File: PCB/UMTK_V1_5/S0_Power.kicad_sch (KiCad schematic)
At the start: 12 parts, among them J4 Power IN, J5 PJ-102BH, U4 LM2576HVS-5, U5 LD1117AS33TR

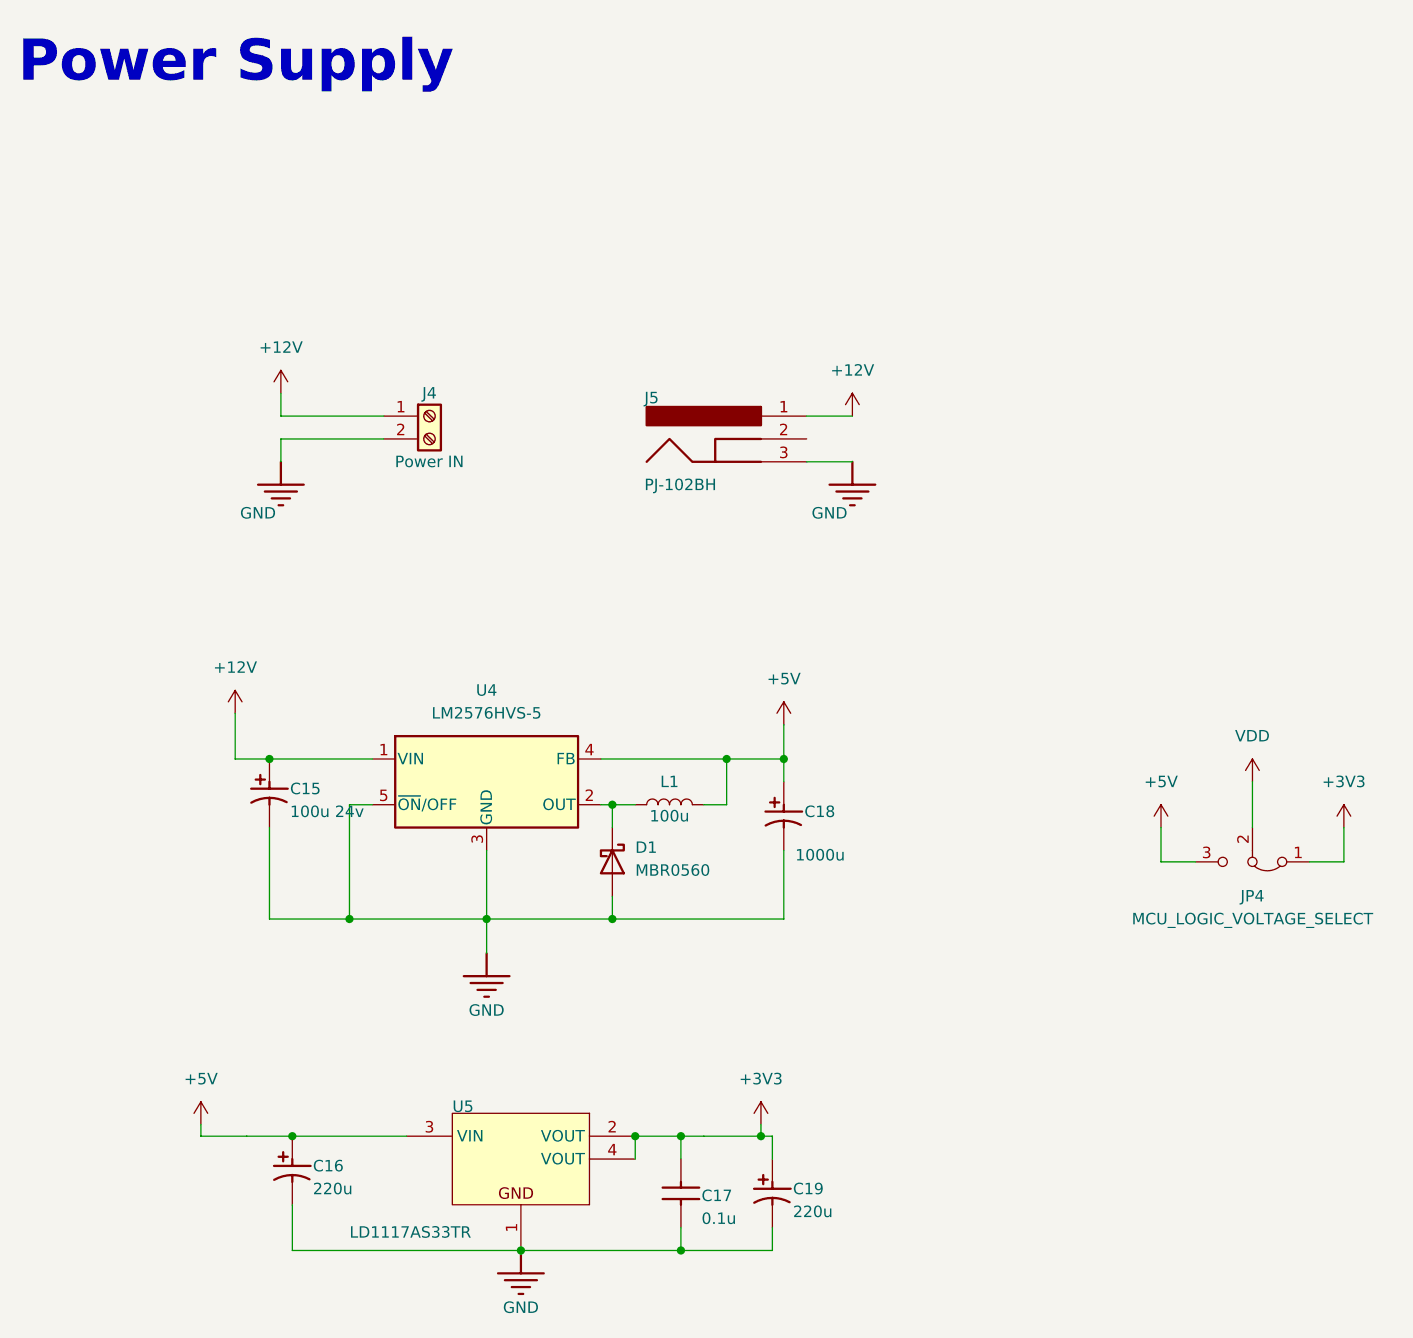
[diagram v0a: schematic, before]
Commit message: Schematic Done, Assigning footprint
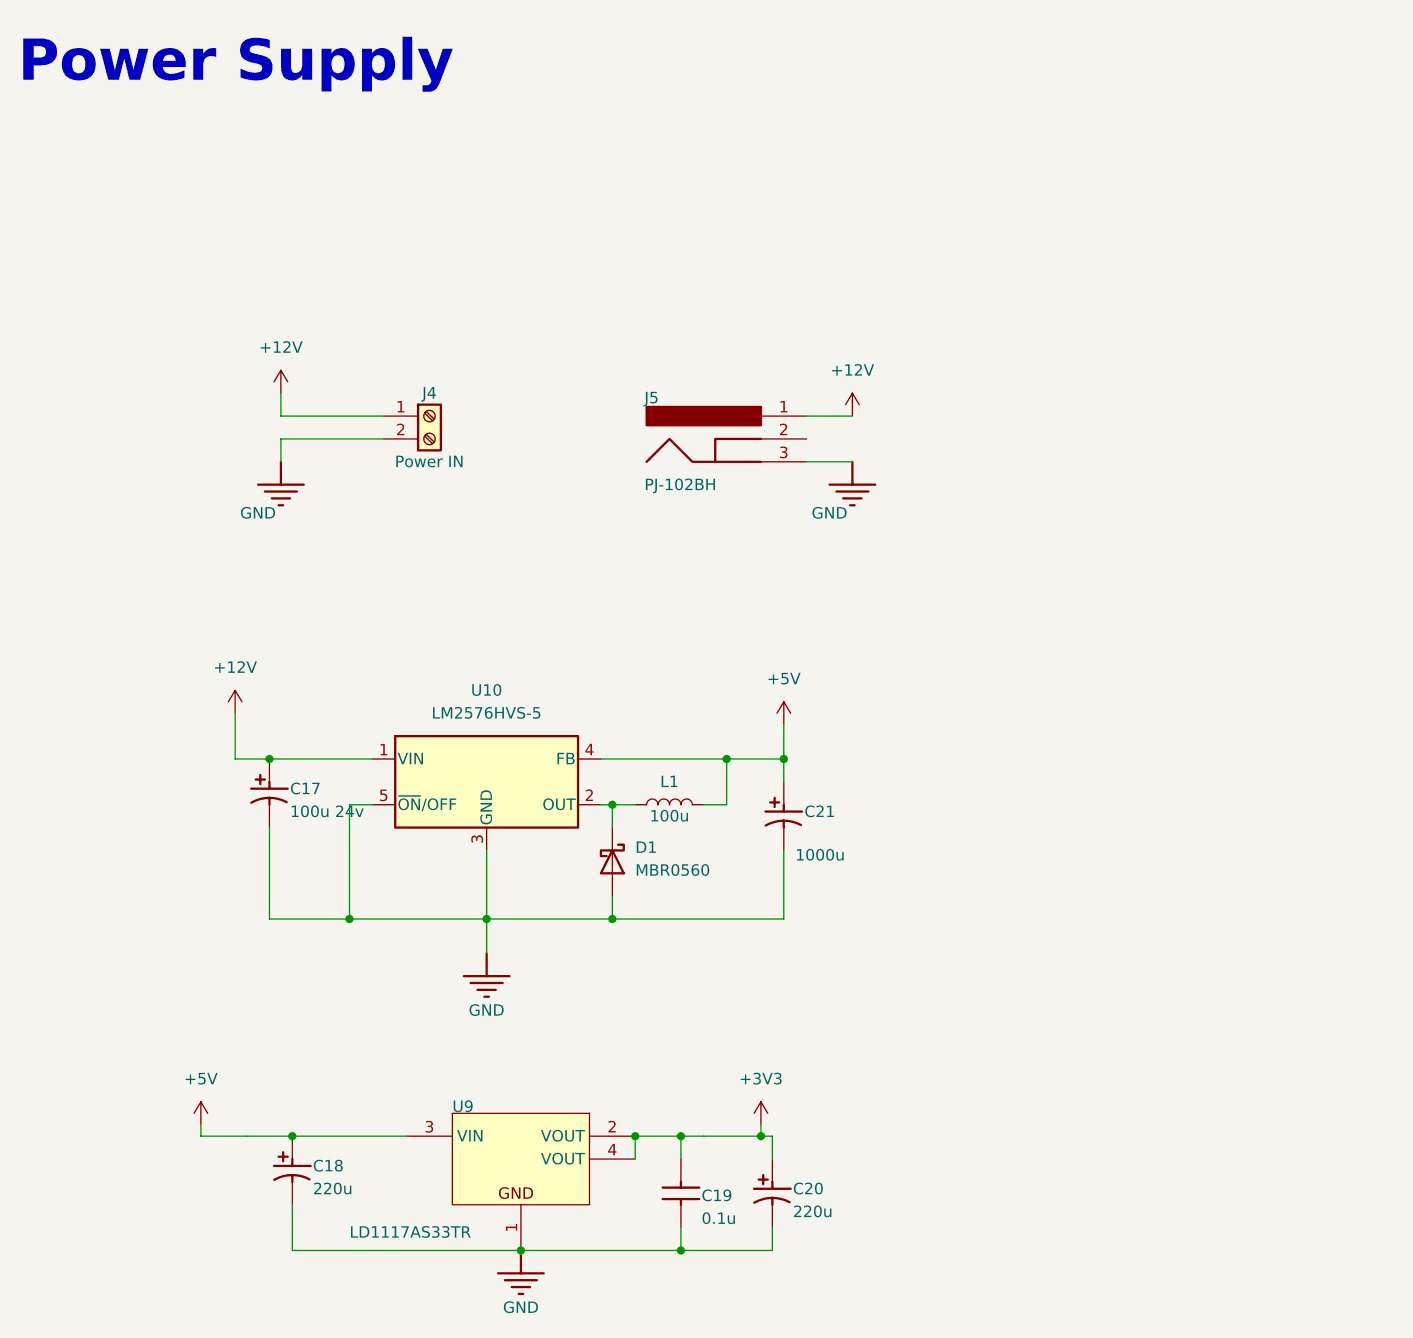
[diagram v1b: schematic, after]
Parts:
- removed JP4: MCU_LOGIC_VOLTAGE_SELECT, symbol Jumper:Jumper_3_Bridged12
- renumbered C15 to C17, C16 to C18, C17 to C19, C19 to C20, C18 to C21, U4 to U10, U5 to U9

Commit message: Footprint assign
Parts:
- added C22: 1000u, Alu Cap 6.3x2.5mm, symbol UMTK-altium-import:0_Polar Cap
- C17: footprint Alu Cap 6.3x2.5mm -> Capacitor_SMD:CP_Elec_10x10.5
- C18: footprint Alu Cap 6.3x2.5mm -> Capacitor_SMD:CP_Elec_8x6.5
- C19: footprint Ceramic Cap 5mm -> Capacitor_SMD:C_0402_1005Metric
- C20, C21: footprint Alu Cap 6.3x2.5mm -> Capacitor_SMD:CP_Elec_10x10
- J4: footprint (none) -> TerminalBlock_Altech:Altech_AK100_1x02_P5.00mm
- J5: footprint CUI-PJ-102BH_V -> digikey-footprints:Barrel_Jack_5.5mmODx2.1mmID_PJ-102A
- L1: footprint (none) -> Inductor_SMD:L_Sunlord_MWSA1206S-101
- U9: footprint SOT-223_M -> Package_TO_SOT_SMD:SOT-223
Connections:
- net +5V: now also C22.1
- net GND: now also C22.2
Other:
- moved on the sheet: C17
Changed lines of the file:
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@@
+	)
+	(junction
+		(at 100.33 113.03)
+		(diameter 0)
+		(color 0 0 0 0)
 	)
 	(junction
@@
 	)
 	(junction
-		(at 43.18 95.25)
-		(diameter 0)
-		(color 0 0 0 0)
-	)
-	(junction
 		(at 97.79 137.16)
 		(diameter 0)
@@
 	)
 	(junction
+		(at 39.37 95.25)
+		(diameter 0)
+		(color 0 0 0 0)
+	)
+	(junction
 		(at 100.33 95.25)
 		(diameter 0)
@@
 	(wire
 		(pts
-			(xy 43.18 102.87) (xy 43.18 113.03)
+			(xy 39.37 105.41) (xy 39.37 113.03)
 		)
 		(stroke
@@
 	(wire
 		(pts
+			(xy 100.33 95.25) (xy 111.76 95.25)
+		)
+		(stroke
+			(width 0)
+			(type default)
+		)
+	)
+	(wire
+		(pts
 			(xy 88.9 137.16) (xy 91.44 137.16)
 		)
@@
 	(wire
 		(pts
-			(xy 43.18 95.25) (xy 54.61 95.25)
-		)
-		(stroke
-			(width 0)
-			(type default)
-		)
-	)
-	(wire
-		(pts
 			(xy 39.37 90.17) (xy 39.37 95.25)
 		)
@@
 	(wire
 		(pts
+			(xy 111.76 95.25) (xy 111.76 97.79)
+		)
+		(stroke
+			(width 0)
+			(type default)
+		)
+	)
+	(wire
+		(pts
 			(xy 88.9 147.32) (xy 88.9 149.86)
 		)
@@
 	(wire
 		(pts
-			(xy 39.37 95.25) (xy 43.18 95.25)
+			(xy 39.37 95.25) (xy 54.61 95.25)
 		)
 		(stroke
@@
 	(wire
 		(pts
+			(xy 39.37 97.79) (xy 39.37 95.25)
+		)
+		(stroke
+			(width 0)
+			(type default)
+		)
+	)
+	(wire
+		(pts
+			(xy 100.33 113.03) (xy 111.76 113.03)
+		)
+		(stroke
+			(width 0)
+			(type default)
+		)
+	)
+	(wire
+		(pts
 			(xy 44.45 57.15) (xy 55.88 57.15)
 		)
@@
 	(wire
 		(pts
+			(xy 111.76 105.41) (xy 111.76 113.03)
+		)
+		(stroke
+			(width 0)
+			(type default)
+		)
+	)
+	(wire
+		(pts
 			(xy 83.82 139.7) (xy 83.82 137.16)
 		)
@@
 	(wire
 		(pts
-			(xy 52.07 113.03) (xy 43.18 113.03)
+			(xy 52.07 113.03) (xy 39.37 113.03)
 		)
 		(stroke
@@
 			)
 		)
-		(property "Footprint" "Alu Cap 6.3x2.5mm"
+		(property "Footprint" "Capacitor_SMD:CP_Elec_10x10"
 			(at 99.06 139.7 0)
 			(effects
@@
 			)
 		)
-		(property "Footprint" "CUI-PJ-102BH_V"
+		(property "Footprint" "digikey-footprints:Barrel_Jack_5.5mmODx2.1mmID_PJ-102A"
 			(at 85.09 57.15 0)
 			(effects
@@
 			)
 		)
-		(property "Footprint" ""
+		(property "Footprint" "TerminalBlock_Altech:Altech_AK100_1x02_P5.00mm"
 			(at 60.96 57.15 0)
 			(effects
@@
 			)
 		)
-		(property "Footprint" "Ceramic Cap 5mm"
+		(property "Footprint" "Capacitor_SMD:C_0402_1005Metric"
 			(at 88.9 139.7 0)
 			(effects
@@
 				(path "/2bf3ea67-58b8-47b3-a768-ea6950b40edf/9034045e-70ca-44cd-84b0-62f91947c95b"
 					(reference "C19")
+					(unit 1)
+				)
+			)
+		)
+	)
+	(symbol
+		(lib_id "UMTK-altium-import:0_Polar Cap")
+		(at 111.76 97.79 0)
+		(unit 1)
+		(exclude_from_sim no)
+		(in_bom yes)
+		(on_board yes)
+		(dnp no)
+		(property "Reference" "C22"
+			(at 114.046 101.854 0)
+			(effects
+				(font
+					(size 1.27 1.27)
+				)
+				(justify left bottom)
+			)
+		)
+		(property "Value" "1000u"
+			(at 113.03 106.68 0)
+			(effects
+				(font
+					(size 1.27 1.27)
+				)
+				(justify left bottom)
+			)
+		)
+		(property "Footprint" "Alu Cap 6.3x2.5mm"
+			(at 111.76 97.79 0)
+			(effects
+				(font
+					(size 1.27 1.27)
+				)
+				(hide yes)
+			)
+		)
+		(property "Datasheet" ""
+			(at 111.76 97.79 0)
+			(effects
+				(font
+					(size 1.27 1.27)
+				)
+				(hide yes)
+			)
+		)
+		(property "Description" ""
+			(at 111.76 97.79 0)
+			(effects
+				(font
+					(size 1.27 1.27)
+				)
+				(hide yes)
+			)
+		)
+		(pin "1"
+		)
+		(pin "2"
+		)
+		(instances
+			(project "UMTK"
+				(path "/2bf3ea67-58b8-47b3-a768-ea6950b40edf/9034045e-70ca-44cd-84b0-62f91947c95b"
+					(reference "C22")
 					(unit 1)
 				)
@@
 			)
 		)
-		(property "Footprint" ""
+		(property "Footprint" "Inductor_SMD:L_Sunlord_MWSA1206S-101"
 			(at 87.63 100.33 0)
 			(effects
@@
 	(symbol
 		(lib_id "UMTK-altium-import:0_Polar Cap")
-		(at 43.18 95.25 0)
+		(at 39.37 97.79 0)
 		(unit 1)
 		(exclude_from_sim no)
@@
 		(dnp no)
 		(property "Reference" "C17"
-			(at 45.466 99.314 0)
+			(at 41.656 101.854 0)
 			(effects
 				(font
@@
 		)
 		(property "Value" "100u 24v"
-			(at 45.466 101.854 0)
-			(effects
-				(font
-					(size 1.27 1.27)
-				)
-				(justify left bottom)
-			)
-		)
-		(property "Footprint" "Alu Cap 6.3x2.5mm"
-			(at 43.18 95.25 0)
+			(at 41.656 104.394 0)
+			(effects
+				(font
+					(size 1.27 1.27)
+				)
+				(justify left bottom)
+			)
+		)
+		(property "Footprint" "Capacitor_SMD:CP_Elec_10x10.5"
+			(at 39.37 97.79 0)
 			(effects
 				(font
@@
 		)
 		(property "Datasheet" ""
-			(at 43.18 95.25 0)
+			(at 39.37 97.79 0)
 			(effects
 				(font
@@
 		)
 		(property "Description" ""
-			(at 43.18 95.25 0)
+			(at 39.37 97.79 0)
 			(effects
 				(font
@@
 			)
 		)
-		(property "Footprint" "Alu Cap 6.3x2.5mm"
+		(property "Footprint" "Capacitor_SMD:CP_Elec_10x10"
 			(at 100.33 97.79 0)
 			(effects
@@
 			)
 		)
-		(property "Footprint" "Alu Cap 6.3x2.5mm"
+		(property "Footprint" "Capacitor_SMD:CP_Elec_8x6.5"
 			(at 45.72 137.16 0)
 			(effects
@@
 			)
 		)
-		(property "Footprint" "SOT-223_M"
+		(property "Footprint" "Package_TO_SOT_SMD:SOT-223"
 			(at 63.5 134.62 0)
 			(effects

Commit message: ERC good, imported into PCB
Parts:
- C22: footprint Alu Cap 6.3x2.5mm -> Capacitor_SMD:CP_Elec_10x10
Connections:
- net GND: now also J5.2
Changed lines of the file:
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@@
+	)
+	(junction
+		(at 107.95 62.23)
+		(diameter 0)
+		(color 0 0 0 0)
 	)
 	(junction
@@
 	(wire
 		(pts
+			(xy 107.95 59.69) (xy 107.95 62.23)
+		)
+		(stroke
+			(width 0)
+			(type default)
+		)
+	)
+	(wire
+		(pts
 			(xy 99.06 137.16) (xy 99.06 139.7)
 		)
@@
 		(pts
 			(xy 67.31 113.03) (xy 67.31 116.84)
+		)
+		(stroke
+			(width 0)
+			(type default)
+		)
+	)
+	(wire
+		(pts
+			(xy 102.87 59.69) (xy 107.95 59.69)
 		)
 		(stroke
@@
 			)
 		)
-		(property "Description" ""
+		(property "Description" "Through Hole Right Angle DC Power Jack, 5 A, 2.5 mm Center Pin, 3 Position, -25 to 85 degC, RoHS, Bulk"
 			(at 85.09 57.15 0)
 			(effects
@@
 			)
 		)
-		(property "Description" ""
+		(property "Description" "Power symbol creates a global label with name \"+12V\""
 			(at 107.95 57.15 0)
 			(effects
@@
 			)
 		)
-		(property "Description" ""
+		(property "Description" "Power symbol creates a global label with name 'GND'"
 			(at 67.31 116.84 0)
 			(effects
@@
 			)
 		)
-		(property "Description" ""
+		(property "Description" "Generic screw terminal, single row, 01x02, script generated (kicad-library-utils/schlib/autogen/connector/)"
 			(at 60.96 57.15 0)
 			(effects
@@
 			)
 		)
-		(property "Footprint" "Alu Cap 6.3x2.5mm"
+		(property "Footprint" "Capacitor_SMD:CP_Elec_10x10"
 			(at 111.76 97.79 0)
 			(effects
@@
 			)
 		)
-		(property "Description" ""
+		(property "Description" "Power symbol creates a global label with name \"+3V3\""
 			(at 97.79 135.89 0)
 			(effects
@@
 			)
 		)
-		(property "Description" ""
+		(property "Description" "Power symbol creates a global label with name \"+5V\""
 			(at 100.33 91.44 0)
 			(effects
@@
 			)
 		)
-		(property "Description" ""
+		(property "Description" "5V 3A, SIMPLE SWITCHER® Step-Down Voltage Regulator, High Voltage Input, TO-263"
 			(at 67.31 97.79 0)
 			(effects
@@
 			)
 		)
-		(property "Description" ""
+		(property "Description" "Inductor"
 			(at 87.63 100.33 0)
 			(effects
@@
 			)
 		)
-		(property "Description" ""
+		(property "Description" "Power symbol creates a global label with name 'GND'"
 			(at 71.12 149.86 0)
 			(effects
@@
 			)
 		)
-		(property "Description" ""
+		(property "Description" "Power symbol creates a global label with name 'GND'"
 			(at 107.95 62.23 0)
 			(effects
@@
 			)
 		)
-		(property "Description" ""
+		(property "Description" "Power symbol creates a global label with name \"+12V\""
 			(at 44.45 54.61 0)
 			(effects
@@
 			)
 		)
-		(property "Description" ""
+		(property "Description" "60V 0.5A Schottky Power Rectifier Diode, SOD-123"
 			(at 81.28 106.68 0)
 			(effects
@@
 			)
 		)
-		(property "Description" ""
+		(property "Description" "1A, Low Drop Positive Voltage Regulator, 3.3V, 4-Pin SOT-223, Tape and Reel"
 			(at 63.5 134.62 0)
 			(effects
@@
 			)
 		)
-		(property "Description" ""
+		(property "Description" "Power symbol creates a global label with name \"+5V\""
 			(at 35.56 135.89 0)
 			(effects
@@
 			)
 		)
-		(property "Description" ""
+		(property "Description" "Power symbol creates a global label with name 'GND'"
 			(at 44.45 62.23 0)
 			(effects
@@
 			)
 		)
-		(property "Description" ""
+		(property "Description" "Power symbol creates a global label with name \"+12V\""
 			(at 39.37 90.17 0)
 			(effects

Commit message: Initial Place, Board Stack
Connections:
- net +12V: now also J4.2 (Pin_2); no longer J4.1 (Pin_1)
- net GND: now also J4.1 (Pin_1); no longer J4.2 (Pin_2)
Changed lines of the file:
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@@
-	)
-	(symbol
-		(lib_id "Connector:Screw_Terminal_01x02")
-		(at 60.96 57.15 0)
-		(unit 1)
-		(exclude_from_sim no)
-		(in_bom yes)
-		(on_board yes)
-		(dnp no)
-		(property "Reference" "J4"
-			(at 60.96 54.61 0)
-			(effects
-				(font
-					(size 1.27 1.27)
-				)
-			)
-		)
-		(property "Value" "Power IN"
-			(at 60.96 62.23 0)
-			(effects
-				(font
-					(size 1.27 1.27)
-				)
-			)
-		)
-		(property "Footprint" "TerminalBlock_Altech:Altech_AK100_1x02_P5.00mm"
-			(at 60.96 57.15 0)
-			(effects
-				(font
-					(size 1.27 1.27)
-				)
-				(hide yes)
-			)
-		)
-		(property "Datasheet" "~"
-			(at 60.96 57.15 0)
-			(effects
-				(font
-					(size 1.27 1.27)
-				)
-				(hide yes)
-			)
-		)
-		(property "Description" "Generic screw terminal, single row, 01x02, script generated (kicad-library-utils/schlib/autogen/connector/)"
-			(at 60.96 57.15 0)
-			(effects
-				(font
-					(size 1.27 1.27)
-				)
-				(hide yes)
-			)
-		)
-		(pin "1"
-		)
-		(pin "2"
-		)
-		(instances
-			(project "UMTK"
-				(path "/2bf3ea67-58b8-47b3-a768-ea6950b40edf/9034045e-70ca-44cd-84b0-62f91947c95b"
-					(reference "J4")
-					(unit 1)
-				)
-			)
-		)
 	)
 	(symbol
@@
 					(unit 1)
 				)
+			)
+		)
+	)
+	(symbol
+		(lib_id "Connector:Screw_Terminal_01x02")
+		(at 60.96 59.69 0)
+		(mirror x)
+		(unit 1)
+		(exclude_from_sim no)
+		(in_bom yes)
+		(on_board yes)
+		(dnp no)
+		(property "Reference" "J4"
+			(at 60.96 62.23 0)
+			(effects
+				(font
+					(size 1.27 1.27)
+				)
+			)
+		)
+		(property "Value" "Power IN"
+			(at 60.96 54.61 0)
+			(effects
+				(font
+					(size 1.27 1.27)
+				)
+			)
+		)
+		(property "Footprint" "TerminalBlock_Altech:Altech_AK100_1x02_P5.00mm"
+			(at 60.96 59.69 0)
+			(effects
+				(font
+					(size 1.27 1.27)
+				)
+				(hide yes)
+			)
+		)
+		(property "Datasheet" "~"
+			(at 60.96 59.69 0)
+			(effects
+				(font
+					(size 1.27 1.27)
+				)
+				(hide yes)
+			)
+		)
+		(property "Description" "Generic screw terminal, single row, 01x02, script generated (kicad-library-utils/schlib/autogen/connector/)"
+			(at 60.96 59.69 0)
+			(effects
+				(font
+					(size 1.27 1.27)
+				)
+				(hide yes)
+			)
+		)
+		(pin "1"
+		)
+		(pin "2"
+		)
+		(instances
+			(project "UMTK"
+				(path "/2bf3ea67-58b8-47b3-a768-ea6950b40edf/9034045e-70ca-44cd-84b0-62f91947c95b"
+					(reference "J4")
+					(unit 1)
+				)

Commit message: Layout Continue
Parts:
- removed C18: 220u, Capacitor_SMD:CP_Elec_8x6.5, symbol UMTK-altium-import:0_Polar Cap
- removed C19: 0.1u, Capacitor_SMD:C_0402_1005Metric, symbol UMTK-altium-import:0_Cap
- removed C20: 220u, Capacitor_SMD:CP_Elec_10x10, symbol UMTK-altium-import:0_Polar Cap
- removed C22: 1000u, Capacitor_SMD:CP_Elec_10x10, symbol UMTK-altium-import:0_Polar Cap
- removed J4: Power IN, TerminalBlock_Altech:Altech_AK100_1x02_P5.00mm, symbol Connector:Screw_Terminal_01x02
- removed U9: LD1117AS33TR, Package_TO_SOT_SMD:SOT-223, symbol UMTK-altium-import:0_PM-REG-LD1117-SOT4
- added C18, C19: 10u, Capacitor_SMD:C_0805_2012Metric, symbol Device:C
- added U13: TLV76133DCY, Package_TO_SOT_SMD:SOT-223-3_TabPin2, symbol Regulator_Linear:TLV76133DCY
- C21: footprint Capacitor_SMD:CP_Elec_10x10 -> Capacitor_SMD:CP_Elec_8x10.5
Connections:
- net +3V3: now also C19.2, U13.2 (VO)
- net +5V: now also C18.2, U13.3 (VI)
- net GND: now also C18.1, C19.1, U13.1 (GND)

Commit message: Routing and JLC Assignment Done
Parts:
- C17: value 100u 24v -> 100u hv
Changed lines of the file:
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@@
 			)
 		)
-		(property "Value" "100u 24v"
+		(property "Value" "100u hv"
 			(at 41.656 104.394 0)
 			(effects

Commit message: Bug fixes and add dummy headers for DFM
Fix:
- Power jack footprint incorrect for high current jack
- Motor and Estop terminal hole size too small
- Added designator and position for arduino headers for DFM
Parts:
- J5: footprint digikey-footprints:Barrel_Jack_5.5mmODx2.1mmID_PJ-102A -> digikey-footprints:Barrel_Jack_5.5mmODx2.1mmID_PJ-202A
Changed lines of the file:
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@@
 			)
 		)
-		(property "Footprint" "digikey-footprints:Barrel_Jack_5.5mmODx2.1mmID_PJ-102A"
+		(property "Footprint" "digikey-footprints:Barrel_Jack_5.5mmODx2.1mmID_PJ-202A"
 			(at 85.09 57.15 0)
 			(effects
